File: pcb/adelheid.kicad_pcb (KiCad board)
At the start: 2 copper layers, 339.1 x 143.2 mm, 323 parts, among them J1 USB_B_Mini, J12 VCC, J13 D+, J14 D-, J15 GND, J2 MISO, J3 VCC, J4 SCK, J5 MOSI, J6 RES, J7 GND, J8 PF4, J9 PF5, Q1 2N7002, U1 USBLC6-2SC6, U2 ATmega32U4-AU, Y1 Crystal_GND24

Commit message: Converted Adelheid mini USB to Aristutea USB-C
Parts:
- removed  G2: LOGO, adelheid:adelheid-logo
- removed G1: LOGO, adelheid:adelheid-logo
- removed J14: D-, Pin_Headers:Pin_Header_Straight_1x01_Pitch2.54mm
- removed J15: GND, Pin_Headers:Pin_Header_Straight_1x01_Pitch2.54mm
- added J10: D-, Connector_PinHeader_2.54mm:PinHeader_1x01_P2.54mm_Vertical, B.Cu at (149.6, 26.4)
- added J11: D+, Connector_PinHeader_2.54mm:PinHeader_1x01_P2.54mm_Vertical, B.Cu at (146.8, 26.4)
- added R6: 22, Resistor_SMD:R_0805_2012Metric_Pad1.20x1.40mm_HandSolder, B.Cu at (160.8, 29.5)
- added R7: 22, Resistor_SMD:R_0805_2012Metric_Pad1.20x1.40mm_HandSolder, B.Cu at (160.8, 31.5)
- J1: value USB_B_Mini -> USB_C_Receptacle_HRO_TYPE-C-31-M-12; footprint Keebio-Parts:USB-Mini-B_2leg -> arisutea:USB_C_Receptacle_HRO_TYPE-C-31-M-12-HandSoldering
- J12: footprint Pin_Headers:Pin_Header_Straight_1x01_Pitch2.54mm -> Connector_PinHeader_2.54mm:PinHeader_1x01_P2.54mm_Vertical
- J13: value D+ -> GND; footprint Pin_Headers:Pin_Header_Straight_1x01_Pitch2.54mm -> Connector_PinHeader_2.54mm:PinHeader_1x01_P2.54mm_Vertical
- R1, R2: value 22 -> 5K1; footprint Resistor_SMD:R_0805_2012Metric_Pad1.15x1.40mm_HandSolder -> arisutea:R_0805_2012Metric_Pad1.20x1.40mm_HandSolder
- U1: footprint TO_SOT_Packages_SMD:SOT-23-6_Handsoldering -> Package_TO_SOT_SMD:SOT-23-6_Handsoldering
- moved R1 28.1 mm to (188.7, 28.7), turned to 180 degrees
- moved R2 28.1 mm to (188.7, 26.7), turned to 180 degrees
- moved J1 9.86 mm to (175.5, 20.8)
- moved J13 2.29 mm to (144.0, 26.4)
- moved C3 1.27 mm to (184.4, 30.2)
- moved C4 1.27 mm to (182.4, 30.2)
- moved J12 1.02 mm to (152.4, 26.4)
- moved U1 0.25 mm to (166.9, 30.5), turned to 180 degrees
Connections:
- J13 pad 1: Net-(J1-Pad3) -> GND
- R1 pad 1: D+ -> GND
- R1 pad 2: Net-(J1-Pad3) -> Net-(J1-PadA5)
- R2 pad 1: D- -> GND
- R2 pad 2: Net-(J1-Pad2) -> Net-(J1-PadB5)
- U1 pad 1: Net-(U1-Pad1) -> Net-(J1-PadA7)
- U1 pad 3: Net-(U1-Pad3) -> Net-(J1-PadA6)
- U1 pad 4: Net-(J1-Pad2) -> Net-(J11-Pad1)
- U1 pad 6: Net-(J1-Pad3) -> Net-(J10-Pad1)
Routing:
- net Net-(J1-Pad3): track 47.7 -> 0.00 mm, vias 2 -> 0
- net Net-(J1-Pad2): track 40.8 -> 0.00 mm, vias 1 -> 0
- net Net-(J11-Pad1): track 0.00 -> 27.8 mm, vias 0 -> 2
- net Net-(J10-Pad1): track 0.00 -> 24.4 mm
- net Net-(J1-PadA5): track 0.00 -> 16.9 mm, vias 0 -> 2
- net Net-(J1-PadA7): track 0.00 -> 15.5 mm
- net Net-(J1-PadB5): track 0.00 -> 14.9 mm, vias 0 -> 2
- net VCC: track 2646.7 -> 2661.1 mm, vias 15 -> 17
- net Net-(J1-PadA6): track 0.00 -> 13.0 mm
- net GND: track 61.7 -> 64.6 mm
- net Net-(C4-Pad1): track 8.19 -> 9.46 mm
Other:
- board size 339.1 x 143.2 mm -> 339.1 x 145.5 mm

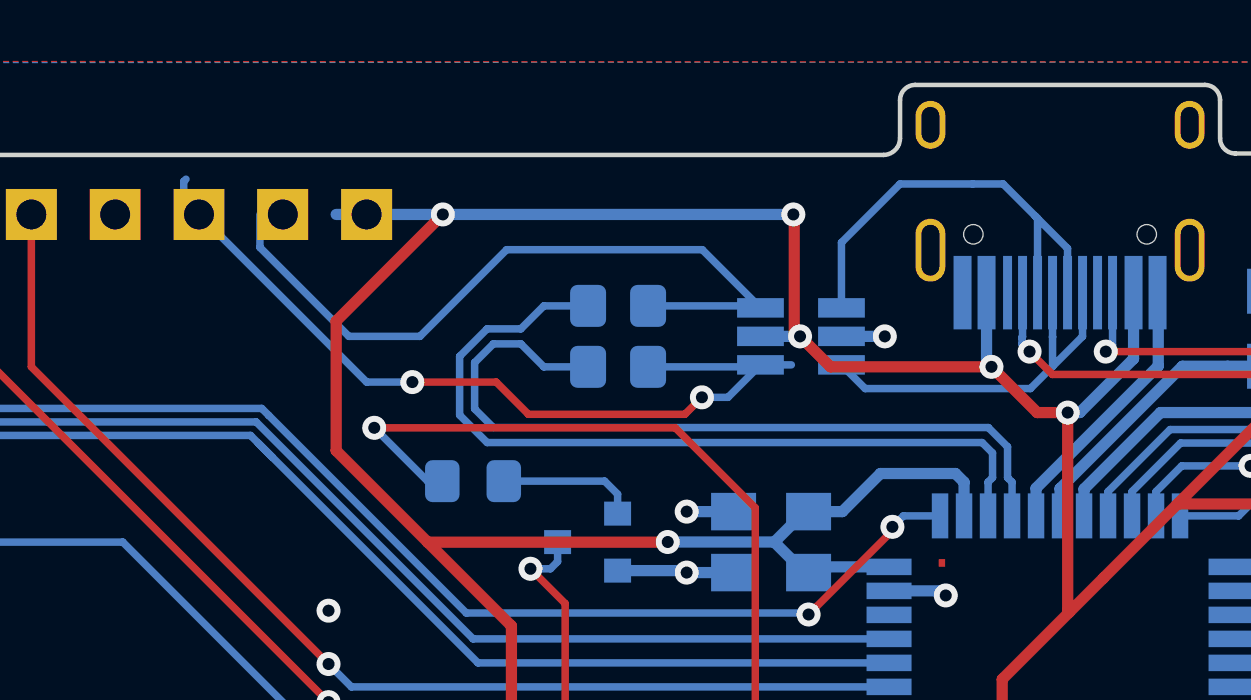
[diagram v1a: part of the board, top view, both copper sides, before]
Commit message: Cleanup a bunch of USB tracks to significantly increase copper fill area
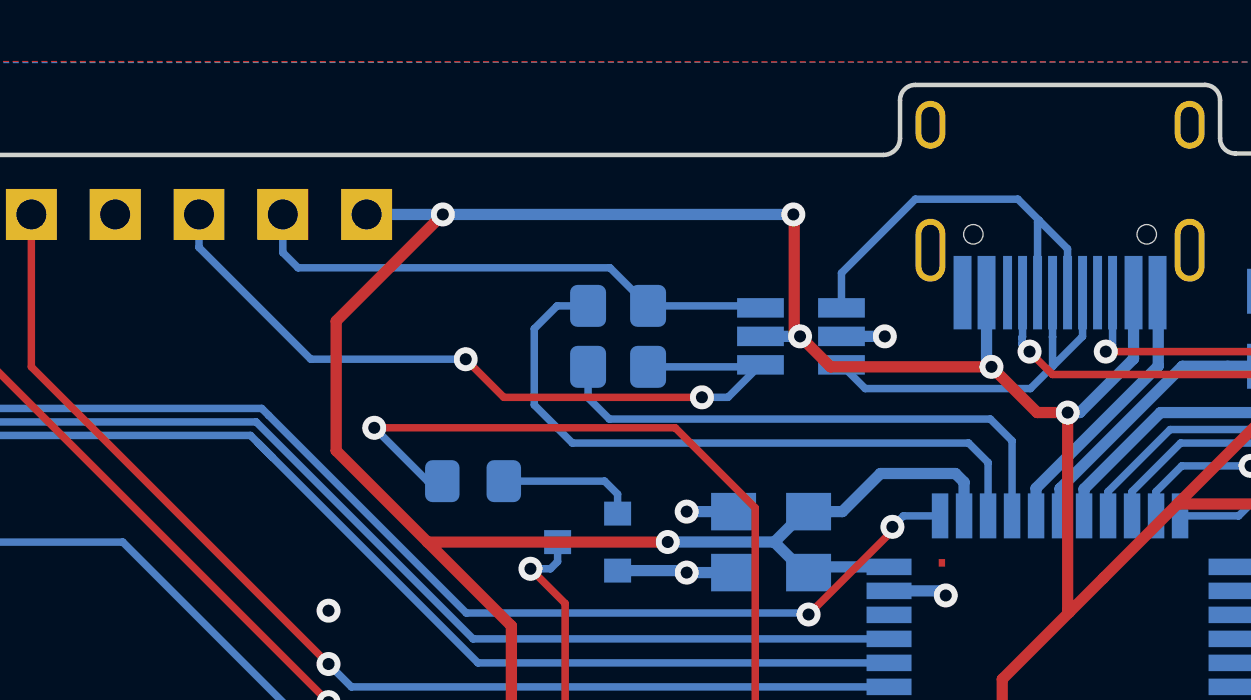
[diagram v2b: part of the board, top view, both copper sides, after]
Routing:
- net D+: track 26.2 -> 18.3 mm
- net Net-(J10-Pad1): track 24.4 -> 17.6 mm
- net D-: track 27.0 -> 22.4 mm
- net Net-(J11-Pad1): track 27.8 -> 25.8 mm
- net Net-(J1-PadA7): track 15.5 -> 14.3 mm
- net VCC: track 2661.1 -> 2660.1 mm

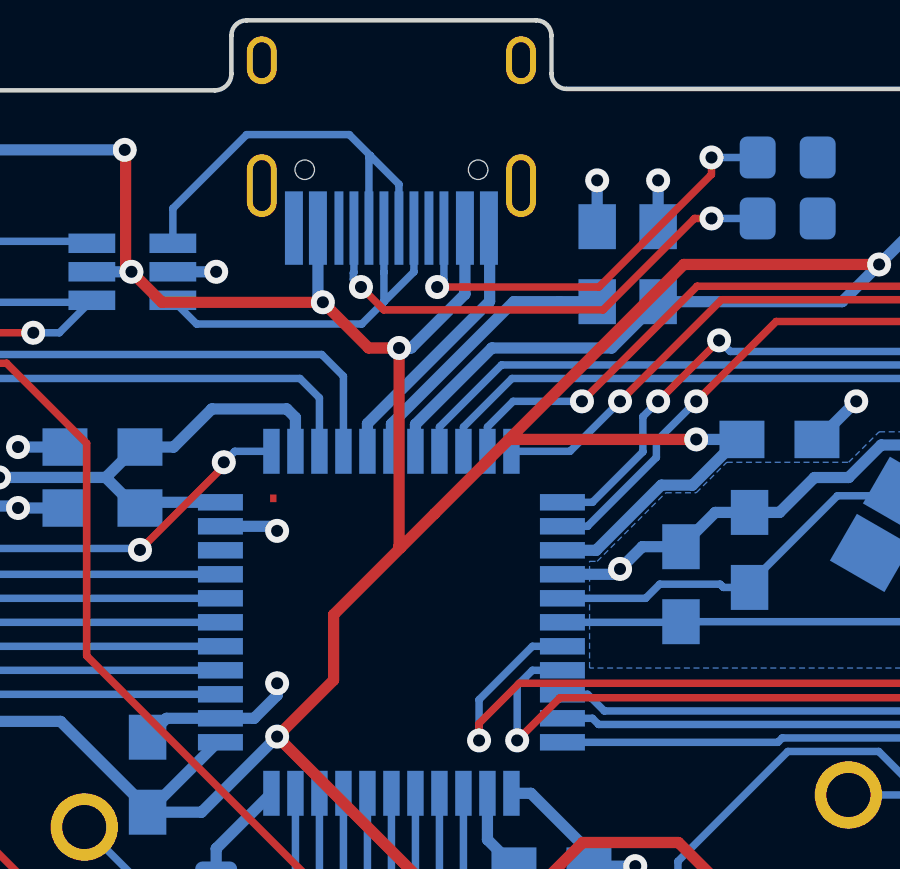
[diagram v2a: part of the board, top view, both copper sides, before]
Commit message: Cleanup a couple more VCC and GND's for the micro.
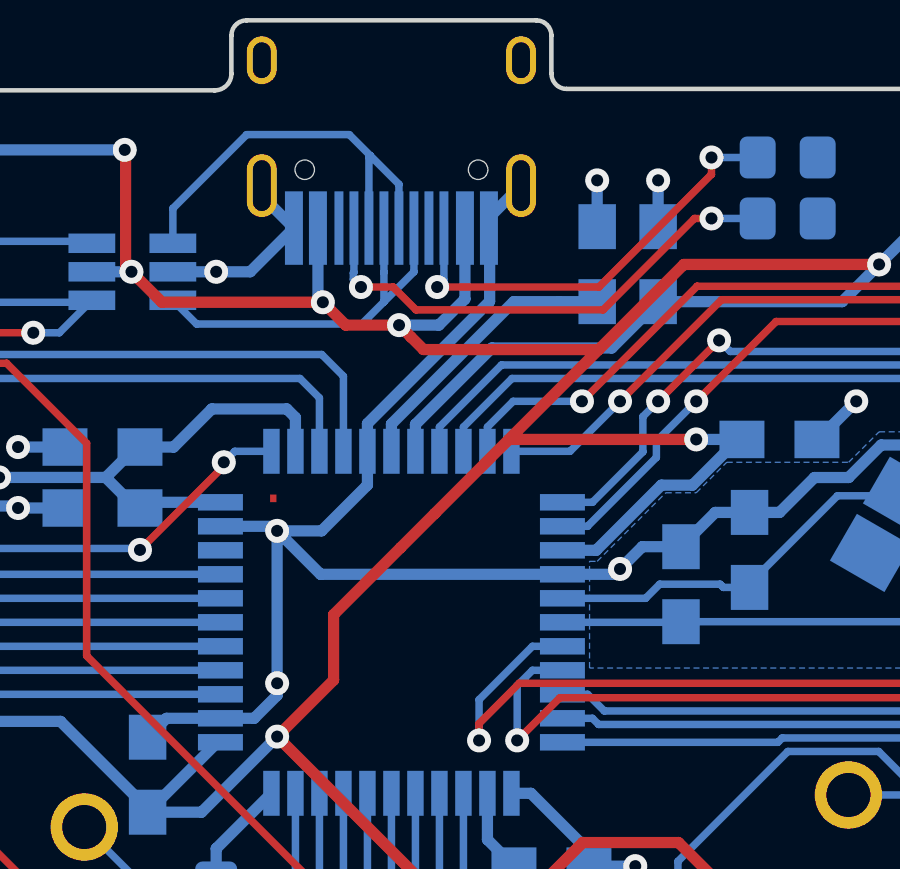
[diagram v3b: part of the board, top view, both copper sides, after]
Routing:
- net GND: track 64.6 -> 91.5 mm
